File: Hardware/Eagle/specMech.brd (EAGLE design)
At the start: 142.2 x 121.9 mm, 78 parts, among them J1 PINHD-1X8-MOLEX-SHROUD, J2 JST-2-PIN-2B-PH-K-S(LF)(SN), J3 PINHD-1X8-MOLEX-SHROUD, J4 PINHD-1X8-MOLEX-SHROUD, J6 Molex 0022232081, J8 Molex 0022232081, U1 MCP23008-E/SO, U10 ADS1115, U11 MCP23008-E/SO, U12 74HC2G17TSSOP-6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

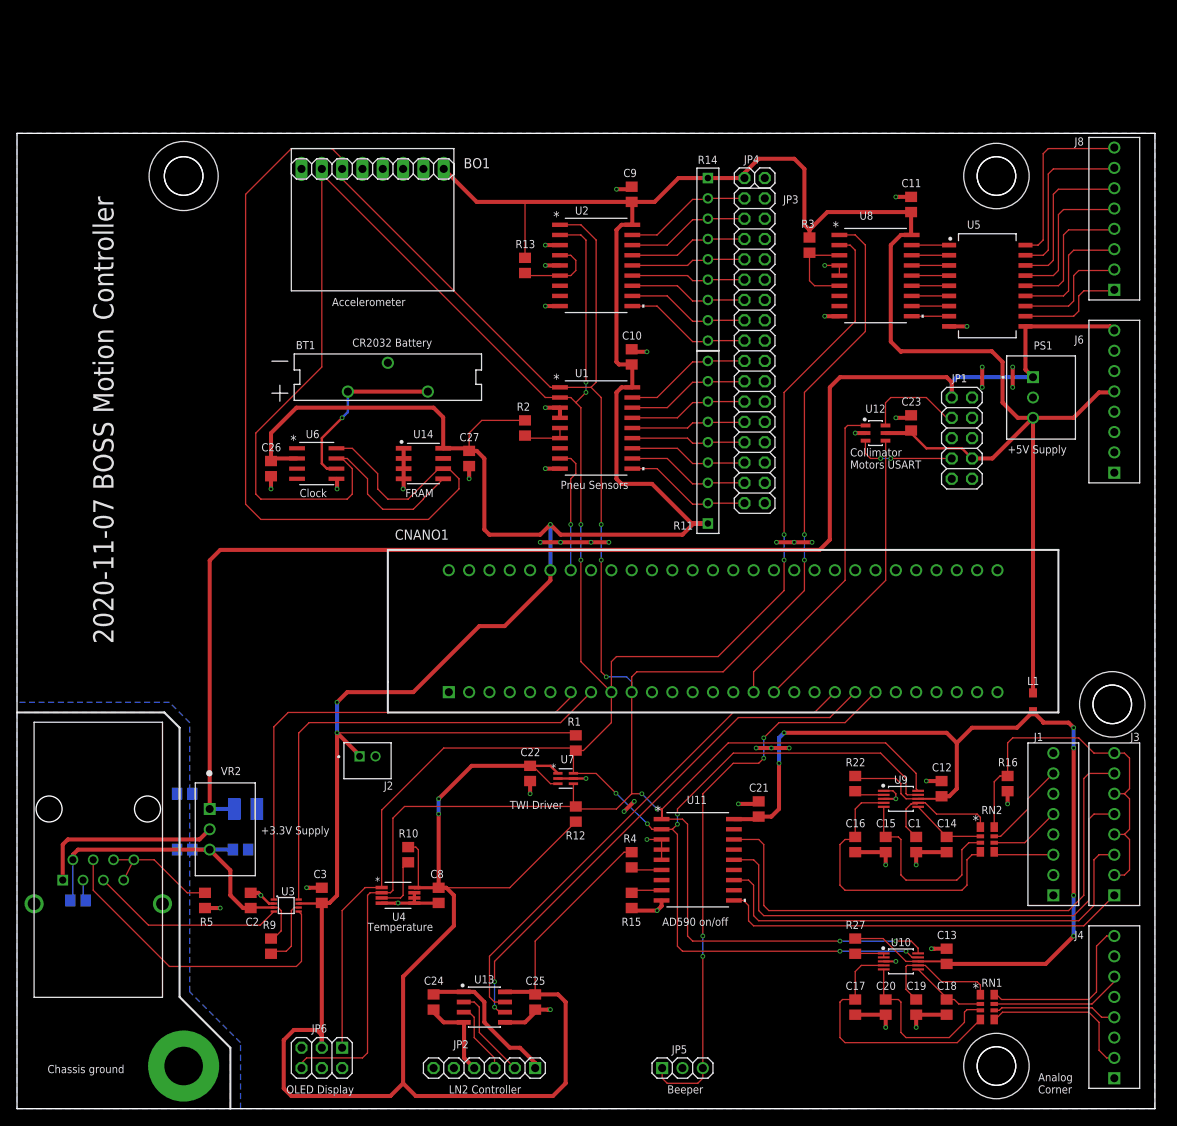
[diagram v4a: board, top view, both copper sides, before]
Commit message: Changed FRAM footprint to allow both IC sizes
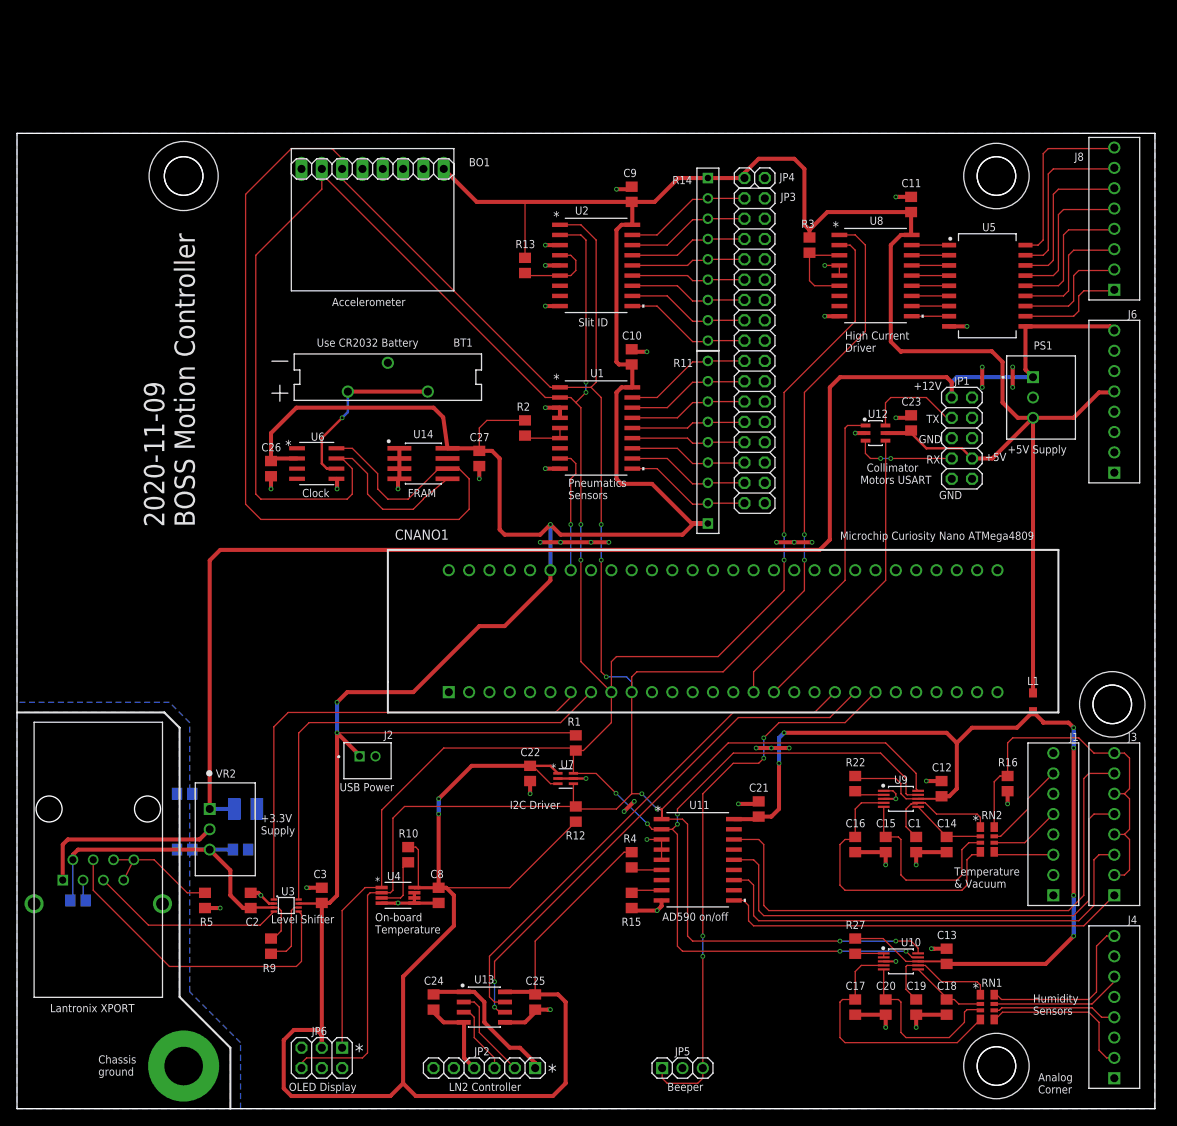
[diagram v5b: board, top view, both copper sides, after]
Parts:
- U14: device AUmlib:SOIC127P600X175-8 -> AUmlib:SOIC127P797X210-8N
- moved C27 1.27 mm to (57.8, 81.3)
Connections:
- removed net INT-SLIT: U2.8
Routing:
- net SCL: track 475.6 -> 479.7 mm
- net +5V: track 636.4 -> 635.0 mm
- net SDA: track 437.6 -> 438.4 mm
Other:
- board text added: "*"
- board text added: "+12V"
- board text added: "+5V"
- board text added: "2020-11-09 BOSS Motion Controller"
- board text added: "GND"
- board text added: "High Current Driver"
- board text added: "Humidity Sensors"
- board text added: "I2C Driver"
- board text added: "Lantronix XPORT"
- board text added: "Level Shifter"
- board text added: "Microchip Curiosity Nano ATMega4809"
- board text added: "On-board Temperature"
- board text added: "Pneumatics Sensors"
- board text added: "RX"
- board text added: "Slit ID"
- board text added: "TX"
- board text added: "Temperature & Vacuum"
- board text added: "USB Power"
- board text added: "Use CR2032 Battery"
- board text removed: "2020-11-07 BOSS Motion Controller"
- board text removed: "CR2032 Battery"
- board text removed: "Pneu Sensors"
- board text removed: "TWI Driver"
- board text removed: "Temperature"

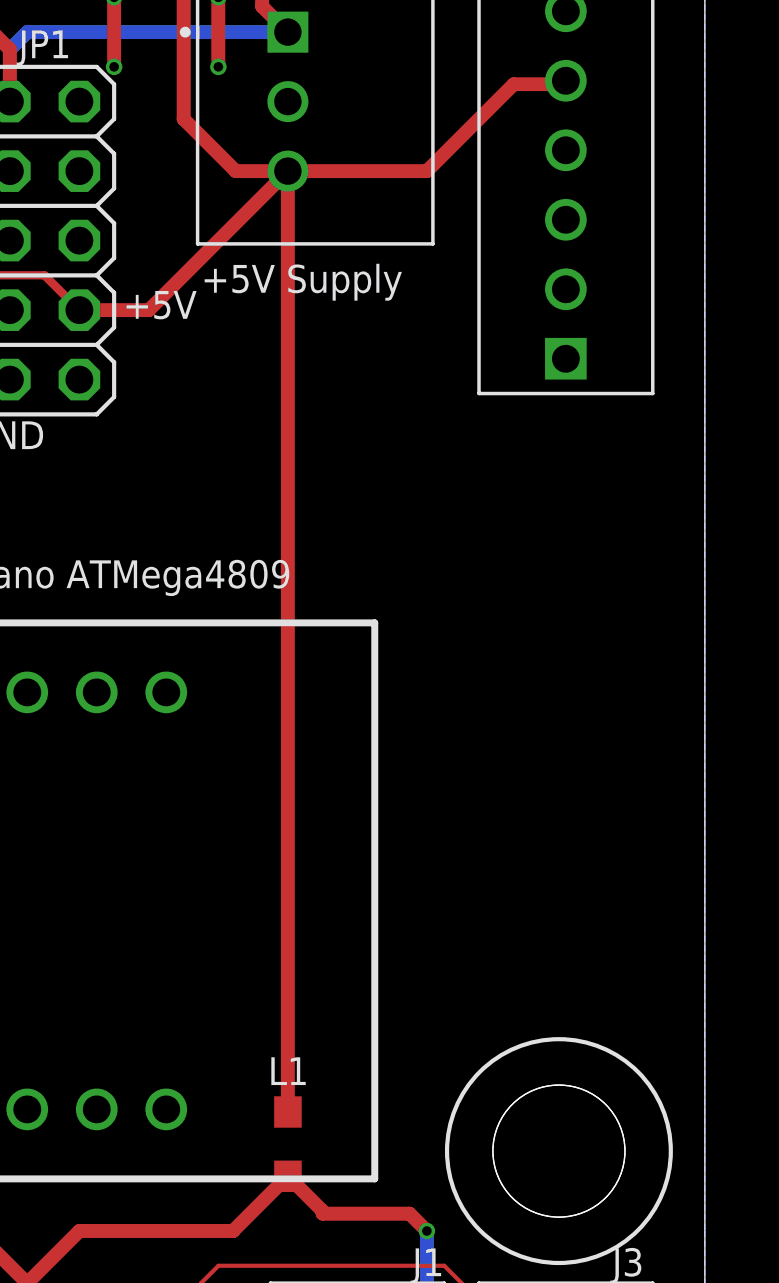
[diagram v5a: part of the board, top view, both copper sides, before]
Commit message: Added spectrograph selection jumper
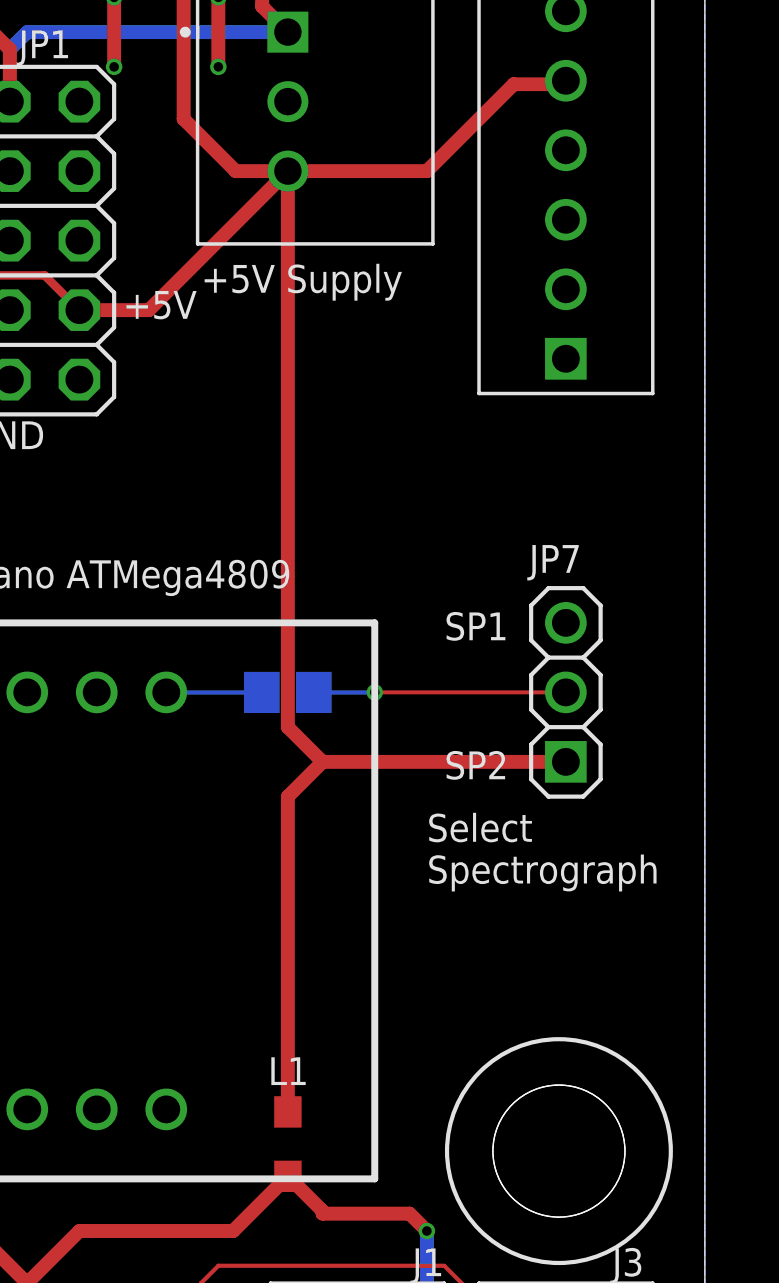
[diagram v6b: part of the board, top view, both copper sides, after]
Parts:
- added JP7: (no value), AUmlib:1X03
- added R6: (no value), AUmlib:R0805
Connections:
- new net N$6: CNANO1.PF2, R6.1
- new net N$7: JP7.2, R6.2
- net +5V: now also JP7.1
- net GND: now also JP7.3
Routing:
- net +5V: track 635.0 -> 644.9 mm
- net N$7: track 0.00 -> 9.21 mm, vias 0 -> 1
- net N$6: track 0.00 -> 3.49 mm
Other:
- board text added: "SP1"
- board text added: "SP2"
- board text added: "Select Spectrograph"

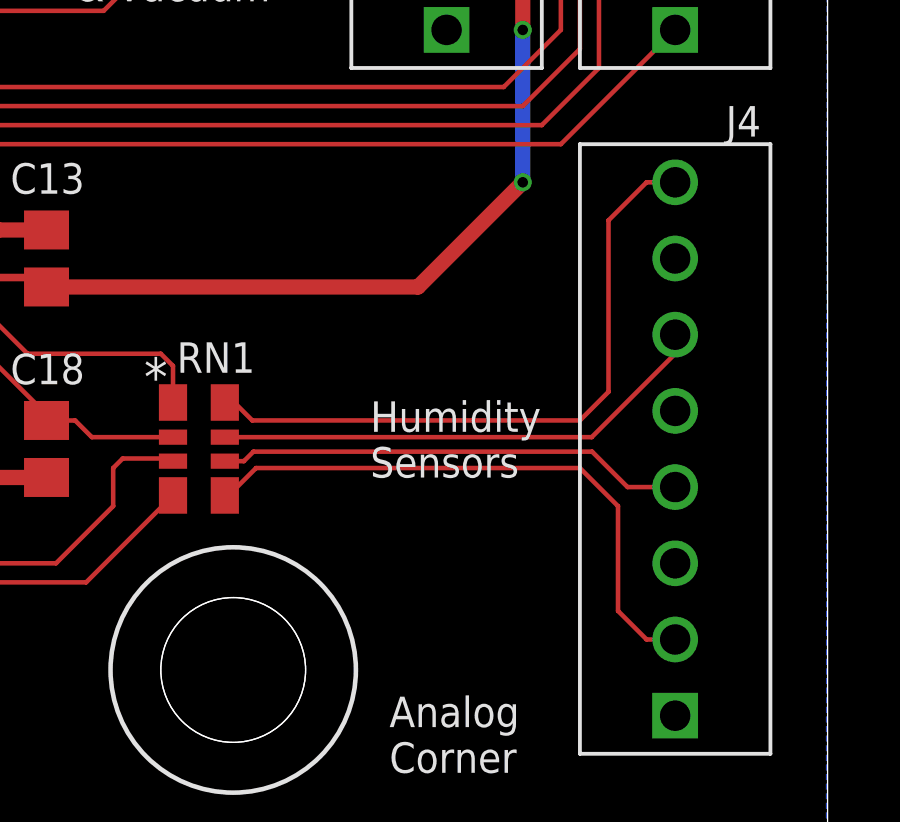
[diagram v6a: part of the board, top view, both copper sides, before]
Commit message: Fixed label errors in humidity sensor input lines
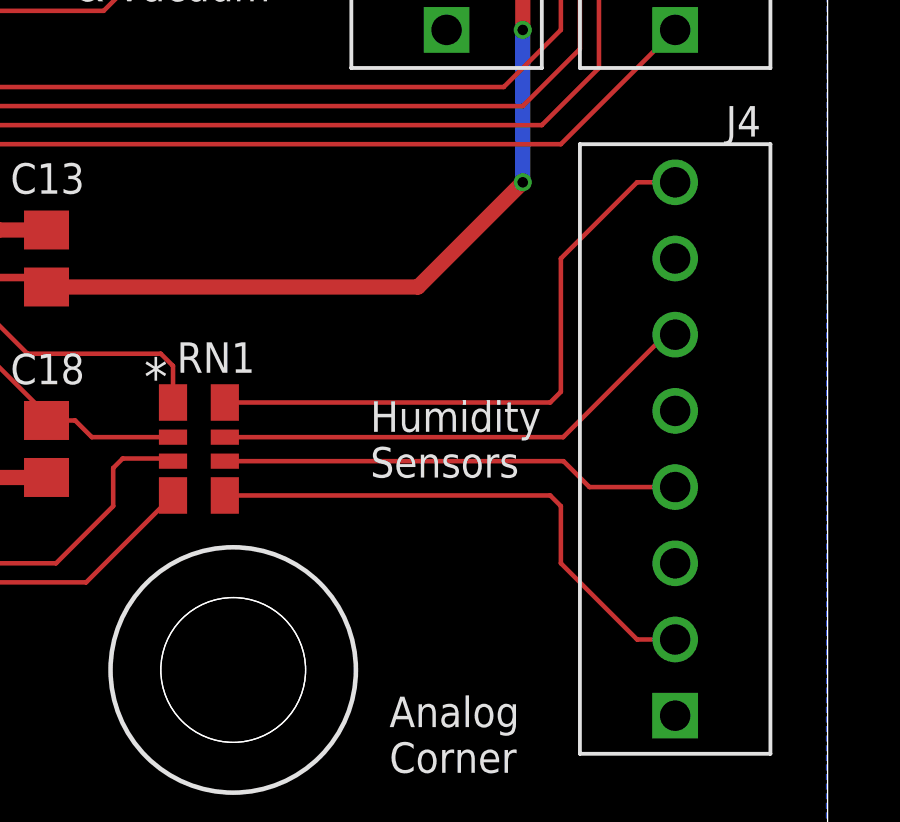
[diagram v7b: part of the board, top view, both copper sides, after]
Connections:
- net A0B: now also J4.P$2, RN1.5; no longer J4.P$8, RN1.8
- net A1B: now also J4.P$4, RN1.6; no longer J4.P$6, RN1.7
- net A2B: now also J4.P$6, RN1.7; no longer J4.P$4, RN1.6
- net A3B: now also J4.P$8, RN1.8; no longer J4.P$2, RN1.5
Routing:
- net A0B: track 21.9 -> 18.1 mm
- net A1B: track 16.8 -> 15.4 mm
- net A3B: track 19.8 -> 20.7 mm
- net A2B: track 15.6 -> 16.4 mm
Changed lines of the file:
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@@
 <setting verticaltext="up"/>
 </settings>
-<grid distance="0.025" unitdist="inch" unit="inch" style="lines" multiple="1" display="yes" altdistance="5" altunitdist="mil" altunit="mil"/>
+<grid distance="0.0125" unitdist="inch" unit="inch" style="lines" multiple="1" display="yes" altdistance="5" altunitdist="mil" altunit="mil"/>
 <layers>
 <layer number="1" name="Top" color="4" fill="1" visible="yes" active="yes"/>
@@
 <wire x1="104.82" y1="19.415" x2="104.775" y2="19.37" width="0.1524" layer="1"/>
 </signal>
-<signal name="A0B">
-<contactref element="RN1" pad="8"/>
-<contactref element="J4" pad="P$8"/>
-<wire x1="123.063" y1="13.6525" x2="122.4661" y2="14.2494" width="0.1524" layer="1"/>
-<wire x1="122.1486" y1="14.2494" x2="122.4661" y2="14.2494" width="0.1524" layer="1"/>
-<wire x1="123.063" y1="13.6525" x2="133.985" y2="13.6525" width="0.1524" layer="1"/>
-<wire x1="133.985" y1="13.6525" x2="134.9375" y2="14.605" width="0.1524" layer="1"/>
-<wire x1="134.9375" y1="14.605" x2="134.9375" y2="20.32" width="0.1524" layer="1"/>
-<wire x1="134.9375" y1="20.32" x2="136.2075" y2="21.59" width="0.1524" layer="1"/>
-<wire x1="136.2075" y1="21.59" x2="137.16" y2="21.59" width="0.1524" layer="1"/>
-</signal>
-<signal name="A1B">
-<contactref element="RN1" pad="7"/>
-<contactref element="J4" pad="P$6"/>
-<wire x1="122.1486" y1="13.0938" x2="134.3788" y2="13.0938" width="0.1524" layer="1"/>
-<wire x1="137.16" y1="15.875" x2="137.16" y2="16.51" width="0.1524" layer="1"/>
-<wire x1="137.16" y1="15.875" x2="134.3788" y2="13.0938" width="0.1524" layer="1"/>
-</signal>
-<signal name="A2B">
-<contactref element="RN1" pad="6"/>
-<contactref element="J4" pad="P$4"/>
-<wire x1="122.1486" y1="12.2938" x2="122.7836" y2="12.2938" width="0.1524" layer="1"/>
-<wire x1="123.1011" y1="12.6113" x2="122.7836" y2="12.2938" width="0.1524" layer="1"/>
-<wire x1="134.3912" y1="12.6113" x2="123.1011" y2="12.6113" width="0.1524" layer="1"/>
-<wire x1="135.5725" y1="11.43" x2="137.16" y2="11.43" width="0.1524" layer="1"/>
-<wire x1="135.5725" y1="11.43" x2="134.3912" y2="12.6113" width="0.1524" layer="1"/>
-</signal>
-<signal name="A3B">
-<contactref element="RN1" pad="5"/>
-<contactref element="J4" pad="P$2"/>
-<wire x1="122.1486" y1="11.1506" x2="122.2756" y2="11.1506" width="0.1524" layer="1"/>
-<wire x1="122.2756" y1="11.1506" x2="123.19" y2="12.065" width="0.1524" layer="1"/>
-<wire x1="123.19" y1="12.065" x2="133.985" y2="12.065" width="0.1524" layer="1"/>
-<wire x1="133.985" y1="12.065" x2="135.255" y2="10.795" width="0.1524" layer="1"/>
-<wire x1="135.255" y1="10.795" x2="135.255" y2="7.3025" width="0.1524" layer="1"/>
-<wire x1="135.255" y1="7.3025" x2="136.2075" y2="6.35" width="0.1524" layer="1"/>
-<wire x1="136.2075" y1="6.35" x2="137.16" y2="6.35" width="0.1524" layer="1"/>
-</signal>
 <signal name="N$66">
 <contactref element="U9" pad="6"/>
@@
 <wire x1="130.175" y1="67.31" x2="137.16" y2="67.31" width="0.1524" layer="1"/>
 </signal>
+<signal name="A0B">
+<contactref element="RN1" pad="5"/>
+<contactref element="J4" pad="P$2"/>
+<wire x1="122.1486" y1="11.1506" x2="132.9944" y2="11.1506" width="0.1524" layer="1"/>
+<wire x1="132.9944" y1="11.1506" x2="133.35" y2="10.795" width="0.1524" layer="1"/>
+<wire x1="133.35" y1="10.795" x2="133.35" y2="8.89" width="0.1524" layer="1"/>
+<wire x1="133.35" y1="8.89" x2="135.89" y2="6.35" width="0.1524" layer="1"/>
+<wire x1="135.89" y1="6.35" x2="137.16" y2="6.35" width="0.1524" layer="1"/>
+</signal>
+<signal name="A1B">
+<contactref element="RN1" pad="6"/>
+<contactref element="J4" pad="P$4"/>
+<wire x1="122.1486" y1="12.2938" x2="133.4387" y2="12.2938" width="0.1524" layer="1"/>
+<wire x1="134.3025" y1="11.43" x2="137.16" y2="11.43" width="0.1524" layer="1"/>
+<wire x1="133.4387" y1="12.2938" x2="134.3025" y2="11.43" width="0.1524" layer="1"/>
+</signal>
+<signal name="A2B">
+<contactref element="RN1" pad="7"/>
+<contactref element="J4" pad="P$6"/>
+<wire x1="122.1486" y1="13.0938" x2="133.4263" y2="13.0938" width="0.1524" layer="1"/>
+<wire x1="136.8425" y1="16.51" x2="137.16" y2="16.51" width="0.1524" layer="1"/>
+<wire x1="133.4263" y1="13.0938" x2="136.8425" y2="16.51" width="0.1524" layer="1"/>
+</signal>
+<signal name="A3B">
+<contactref element="RN1" pad="8"/>
+<contactref element="J4" pad="P$8"/>
+<wire x1="122.1486" y1="14.2494" x2="132.9944" y2="14.2494" width="0.1524" layer="1"/>
+<wire x1="132.9944" y1="14.2494" x2="133.35" y2="14.605" width="0.1524" layer="1"/>
+<wire x1="133.35" y1="14.605" x2="133.35" y2="19.05" width="0.1524" layer="1"/>
+<wire x1="133.35" y1="19.05" x2="135.89" y2="21.59" width="0.1524" layer="1"/>
+<wire x1="135.89" y1="21.59" x2="137.16" y2="21.59" width="0.1524" layer="1"/>
+</signal>
 </signals>
